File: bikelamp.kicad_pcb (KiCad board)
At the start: 2 copper layers, 44 x 46 mm, 43 parts, among them Q2 BSS138, Q3 RBFET, Q4 HIGH, Q5 LOW, Q6 ACFET, SW1 SW_MEC_5E, U1 WT51822-S4AT, U2 RUY0028A

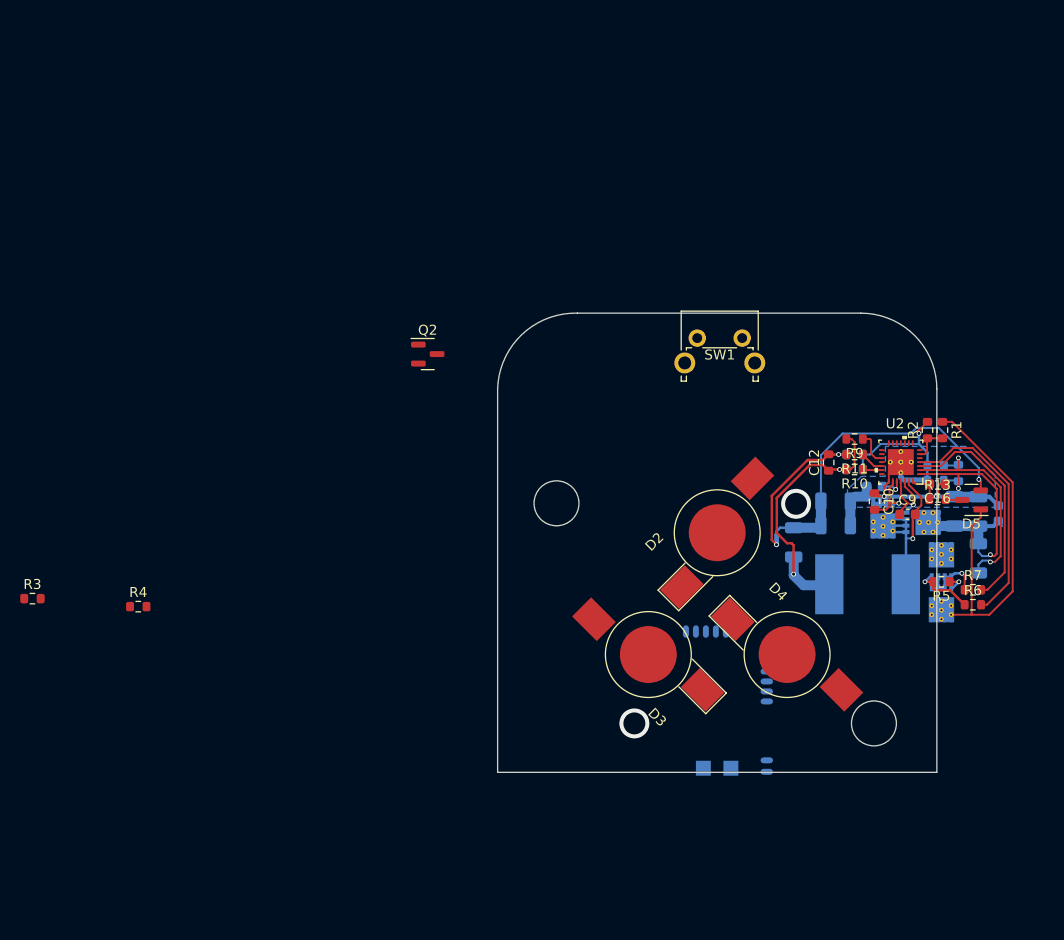
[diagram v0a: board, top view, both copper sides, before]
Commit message: Replaced BLE module with YJ-xxx
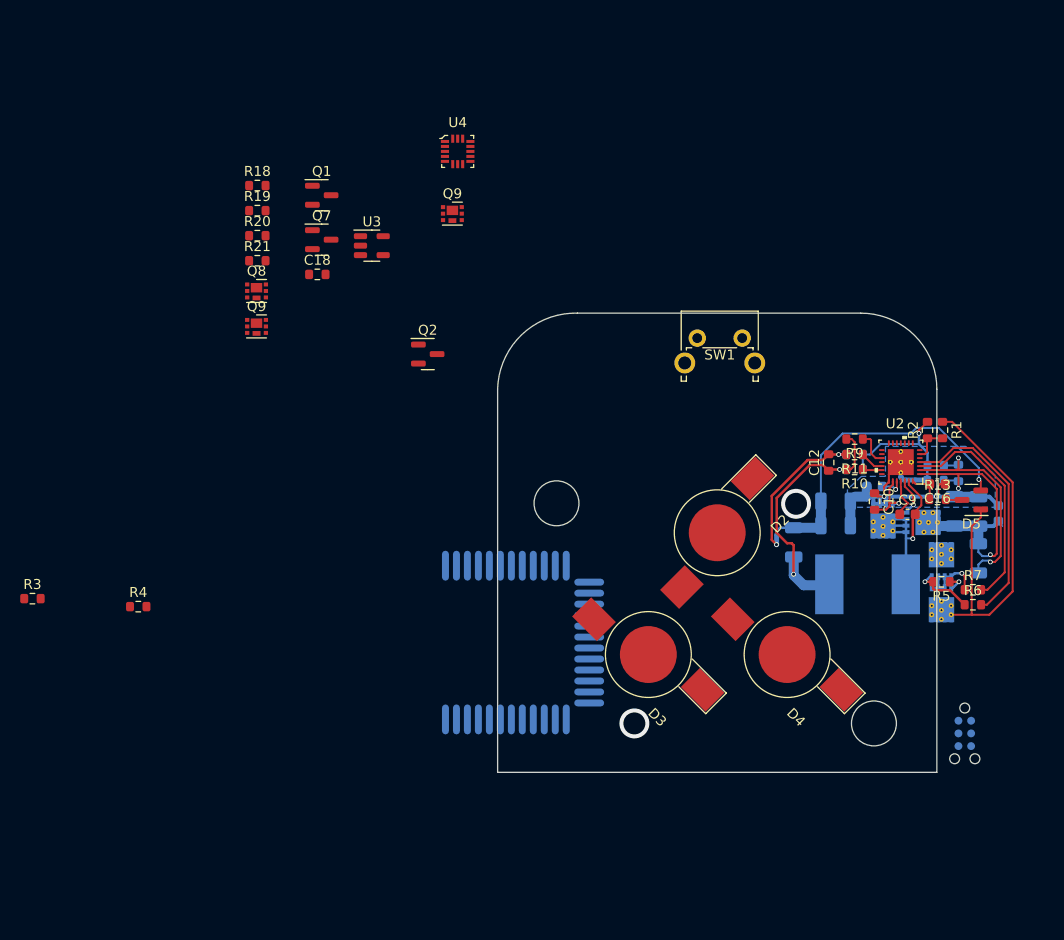
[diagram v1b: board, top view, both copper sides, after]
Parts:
- removed U1: WT51822-S4AT, libs:NRF51822-04
- added C18: 470pF, Resistor_SMD:R_0603_1608Metric, F.Cu at (-30.1, -3.88)
- added J1: Conn_ARM_SWD_TagConnect_TC2030-NL, Connector:Tag-Connect_TC2030-IDC-NL_2x03_P1.27mm_Vertical, B.Cu at (34.8, 42.1)
- added Q1: Q_PMOS_GSD, Package_TO_SOT_SMD:SOT-23, F.Cu at (-29.6, -11.8)
- added Q7: BSS138, Package_TO_SOT_SMD:SOT-23, F.Cu at (-29.6, -7.36)
- added Q8: YJQ3400A-YAN, Package_DFN_QFN:Diodes_UDFN2020-6_Type-F, F.Cu at (-36.1, -2.22)
- added Q9: YJQ3400A-YAN, Package_DFN_QFN:Diodes_UDFN2020-6_Type-F, F.Cu at (-16.5, -9.97)
- added Q9: YJQ3400A-YAN, Package_DFN_QFN:Diodes_UDFN2020-6_Type-F, F.Cu at (-36.1, 1.33)
- added R18: 100, Resistor_SMD:R_0603_1608Metric, F.Cu at (-36.1, -12.8)
- added R19: 100, Resistor_SMD:R_0603_1608Metric, F.Cu at (-36.1, -10.3)
- added R20: 100, Resistor_SMD:R_0603_1608Metric, F.Cu at (-36.1, -7.76)
- added R21: 100, Resistor_SMD:R_0603_1608Metric, F.Cu at (-36.1, -5.25)
- added U3: MIC5205-3.3YM5, Package_TO_SOT_SMD:SOT-23-5, F.Cu at (-24.6, -6.76)
- added U4: MMA8452QR1, digikey-footprints:VQFN-16_3x3mm, F.Cu at (-16.0, -16.2)
- added U5: YJ-14015, footprints:YJ-14015, B.Cu at (-22.8, 33.0)
- U2: value RUY0028A -> BQ24780SRUYR
- turned D2 to -135 degrees
- turned D4 to 135 degrees
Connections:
- net Net-(D5-Pad3) renamed /BQ24780/VCC_R
- net VIN renamed VDD
- D2 pad 1: unconnected-(D2-K) -> Net-(D2-K)
- D2 pad 2: unconnected-(D2-A) -> VBAT
- D3 pad 1: unconnected-(D3-K) -> Net-(D3-K)
- D3 pad 2: unconnected-(D3-A) -> VBAT
- D4 pad 1: unconnected-(D4-K) -> Net-(D4-K)
- D4 pad 2: unconnected-(D4-A) -> VBAT
- SW1 pad 1: unconnected-(SW1-Pad1) -> GND
- SW1 pad 2: unconnected-(SW1-Pad2) -> VBAT
- U2 pad 11: /BQ24780/SDA -> SDA
- U2 pad 12: /BQ24780/SCL -> SCL

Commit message: Working on contours
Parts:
- added C1: C_Polarized_Small, footprints:BQ24780SRUYR, F.Cu at (12.0, -17.7)
- added C19: 100nF, Capacitor_SMD:C_0603_1608Metric, F.Cu at (-1.20, -26.6)
- added C20: 5pF, Capacitor_SMD:C_0603_1608Metric, F.Cu at (-1.20, -24.1)
- added C21: 5pF, Capacitor_SMD:C_0603_1608Metric, F.Cu at (-1.20, -21.6)
- added R22: 1K, Resistor_SMD:R_0603_1608Metric, F.Cu at (-1.20, -19.1)
- added R23: 1K, Resistor_SMD:R_0603_1608Metric, F.Cu at (-1.20, -16.6)
- added R24: 47, Resistor_SMD:R_0603_1608Metric, F.Cu at (-1.20, -14.1)
- added R25: 47, Resistor_SMD:R_0603_1608Metric, F.Cu at (-1.20, -11.6)
- added U1: MCP79402T-xSN, Package_SO:SO-8_3.9x4.9mm_P1.27mm, F.Cu at (5.04, -17.3)
- added U6: MC-306, footprints:MC-306, F.Cu at (6.37, -24.2)
- C10, C11, C12, C13, C18, C3, C4, C5: footprint Resistor_SMD:R_0603_1608Metric -> Capacitor_SMD:C_0603_1608Metric
- C14, C15, C7, C8: footprint Capacitor_SMD:C_1206_3216Metric -> Capacitor_SMD:C_0603_1608Metric
- Q3, Q4, Q5, Q6: footprint libs:CSD18543Q3A -> footprints:CSD18543Q3A
- U2: value BQ24780SRUYR -> RUY0028A; footprint libs:BQ24780SRUYR -> footprints:BQ24780SRUYR
- moved J1 44.6 mm to (-9.60, 46.3), turned to 180 degrees
- moved U5 3.50 mm to (-19.5, 31.9)
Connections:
- U4 pad 11: unconnected-(U4-INT1) -> MMA8452_INT1
- U4 pad 2: unconnected-(U4-BYP) -> Net-(U4-BYP)
- U4 pad 9: unconnected-(U4-INT2) -> MMA8452_INT2
- U5 pad 14: unconnected-(U5-P00) -> LED_PWM_2
- U5 pad 15: unconnected-(U5-P01) -> LED_PWM_1
- U5 pad 16: unconnected-(U5-P02) -> LED_PWM_0
- U5 pad 17: unconnected-(U5-P03) -> WHEEL_SIGNAL
- U5 pad 19: unconnected-(U5-P05) -> SCL
- U5 pad 20: unconnected-(U5-P06) -> SDA
- U5 pad 21: unconnected-(U5-P07) -> PWR_BTN_PRESSED
- U5 pad 22: unconnected-(U5-P08) -> KEEP_POWER
- U5 pad 23: unconnected-(U5-P09) -> MMA8452_INT1
- U5 pad 24: unconnected-(U5-P10) -> MMA8452_INT2
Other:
- board size 44 x 46 mm -> 66.7 x 67.8 mm

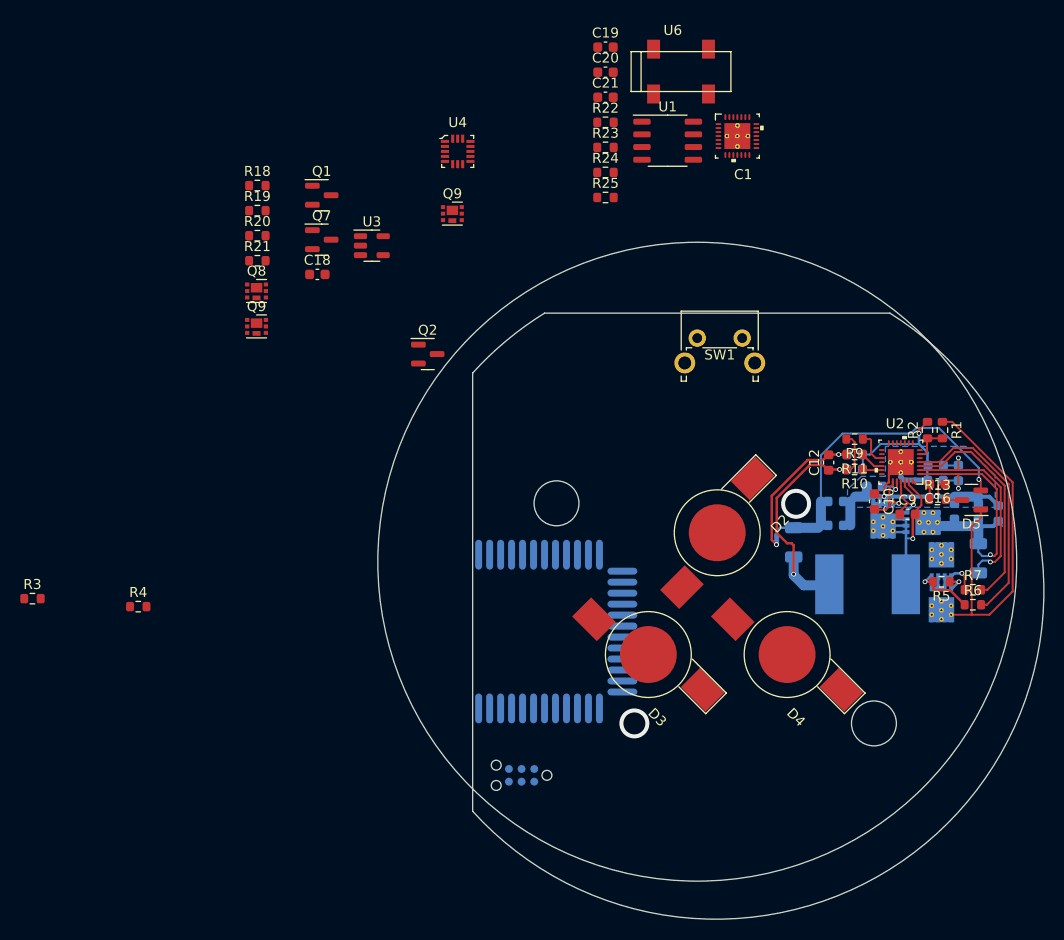
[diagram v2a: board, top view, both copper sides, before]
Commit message: Added gate protection circuit to the SCH
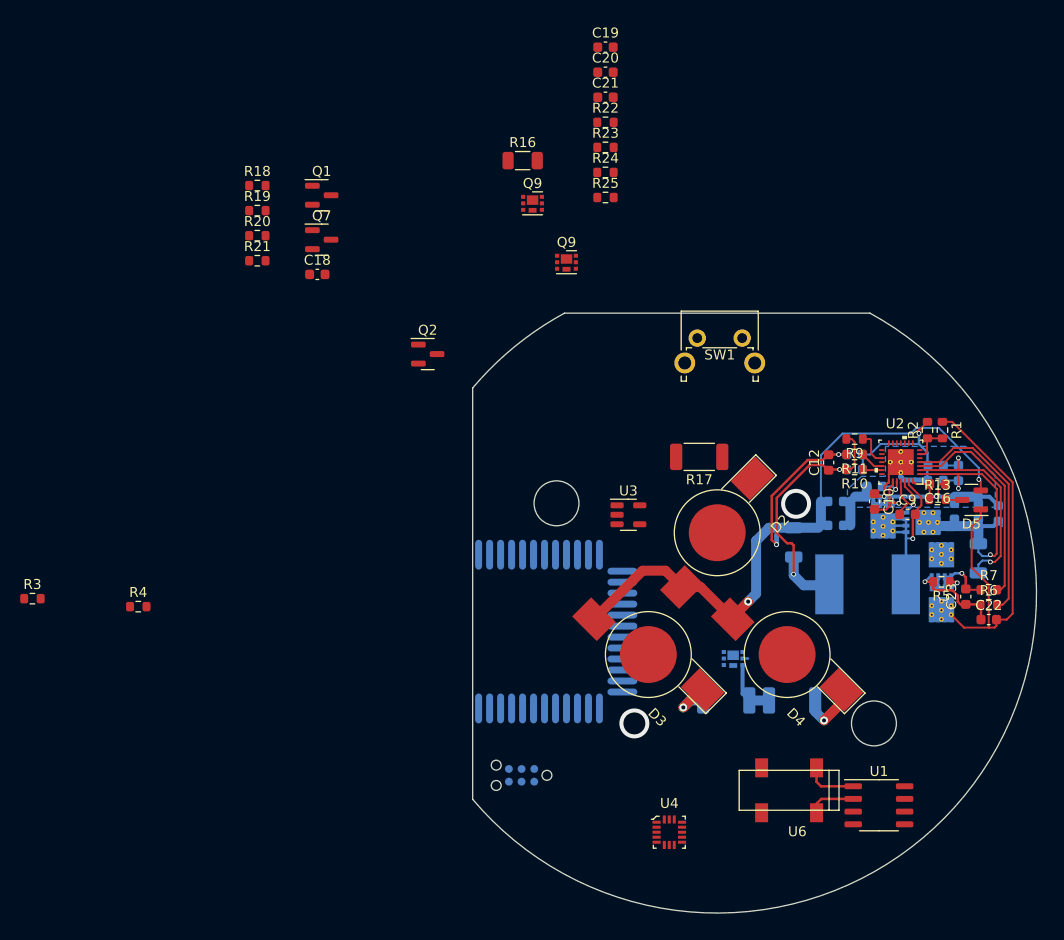
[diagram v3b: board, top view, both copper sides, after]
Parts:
- removed C1: C_Polarized_Small, footprints:BQ24780SRUYR
- added C22: 1nF, Capacitor_SMD:C_0603_1608Metric, F.Cu at (37.2, 30.7)
- added C23: 47nF, Capacitor_SMD:C_0603_1608Metric, F.Cu at (34.9, 28.4)
- added R14: TBD, Resistor_SMD:R_2010_5025Metric, B.Cu at (17.5, 38.8)
- added R15: TBD, Resistor_SMD:R_2010_5025Metric, B.Cu at (10.9, 38.8)
- added R16: TBD, Resistor_SMD:R_1206_3216Metric, F.Cu at (-9.49, -15.3)
- added R17: TBD, Resistor_SMD:R_2010_5025Metric, F.Cu at (8.20, 14.4)
- Q8: moved to B.Cu
- U2: value RUY0028A -> BQ24780SRUYR
- moved U6 72.8 mm to (17.2, 47.8), turned to 180 degrees
- moved U4 71.4 mm to (5.20, 52.0)
- moved U1 69.9 mm to (26.2, 49.3)
- moved Q8 60.3 mm to (11.6, 34.6), turned to 180 degrees
- moved U3 37.2 mm to (1.10, 20.2)
- moved Q9 31.7 mm to (-5.10, -5.10)
- moved Q9 8.10 mm to (-8.50, -11.0)
- moved R6 1.59 mm to (37.2, 29.2)
- moved R7 1.59 mm to (37.2, 27.7)
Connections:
- net ACDET renamed Net-(U2-ACDET)
- net Net-(Q8A-G) renamed /LEDs/LED1_GATE_R
- net Net-(Q8B-G) renamed /LEDs/LED2_GATE_R
- Q9 pad 1: (no net) -> GND
- Q9 pad 2: (no net) -> /LEDs/LED3_GATE_R
- Q9 pad 6: (no net) -> Net-(Q9A-D)
- Q9 pad 2: Net-(Q9A-G) -> /LEDs/LED3_GATE_R
- R20 pad 1: Net-(Q9A-G) -> /LEDs/LED3_GATE_R
- R20 pad 2: /LEDs/LED3_GATE -> LED_PWM_3
- U5 pad 18: unconnected-(U5-P04) -> LED_PWM_3
- U6 pad 1: Net-(U1-X2) -> Net-(U1-X1)
- U6 pad 4: Net-(U1-X1) -> Net-(U1-X2)
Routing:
- net VBAT: track 33.0 -> 64.1 mm, vias 1 -> 2
- net Net-(D4-K): track 0.00 -> 6.15 mm, vias 0 -> 1
- net Net-(Q8B-D): track 0.00 -> 5.80 mm
- net Net-(U1-X1): track 0.00 -> 5.26 mm
- net Net-(D3-K): track 0.00 -> 4.95 mm, vias 0 -> 1
- net Net-(U1-X2): track 0.00 -> 4.78 mm
- net VDD: track 38.5 -> 43.3 mm
- net /BQ24780/RBFET_GATE: track 6.21 -> 9.65 mm
- net /BQ24780/VIN_SWITCHABLE: track 7.78 -> 9.25 mm
- net /BQ24780/CMSRC: track 22.3 -> 21.5 mm
- net /BQ24780/ACDRV: track 24.6 -> 23.9 mm
- net /LEDs/LED1_GATE_R: track 0.00 -> 0.56 mm
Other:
- board size 66.7 x 67.8 mm -> 56.5 x 60.1 mm

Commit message: ERC pass
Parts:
- Q2: moved to B.Cu
- R3: value R_Small -> 1M; moved to B.Cu
- R4: value R_Small -> 3M; moved to B.Cu
- moved R3 98.0 mm to (39.2, 23.8), turned to 180 degrees
- moved R4 87.3 mm to (39.2, 25.3)
- moved Q2 63.0 mm to (39.2, 28.0), turned to -90 degrees
- moved R16 19.4 mm to (-7.00, 4.00)
- moved Q9 14.1 mm to (-3.00, 2.00)
- moved Q9 11.5 mm to (4.00, 2.00)
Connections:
- Q2 pad 1: unconnected-(Q2-G-Pad1) -> Net-(Q2-G)
- Q2 pad 2: unconnected-(Q2-S-Pad2) -> /BQ24780/VIN_SWITCHABLE
- Q2 pad 3: unconnected-(Q2-D-Pad3) -> /BQ24780/RBFET_GATE
- R3 pad 1: unconnected-(R3-Pad1) -> GNDPWR
- R3 pad 2: unconnected-(R3-Pad2) -> Net-(Q2-G)
- R4 pad 1: unconnected-(R4-Pad1) -> Net-(Q2-G)
- R4 pad 2: unconnected-(R4-Pad2) -> /BQ24780/VIN_SWITCHABLE
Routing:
- net /BQ24780/RBFET_GATE: track 9.65 -> 15.9 mm, vias 1 -> 2
- net GNDPWR: track 30.6 -> 36.5 mm
- net Net-(D2-K): track 0.00 -> 3.92 mm
- net Net-(Q2-G): track 0.00 -> 3.31 mm
- net /BQ24780/VIN_SWITCHABLE: track 9.25 -> 11.1 mm

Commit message: Board routed
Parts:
- removed the Q9 at (-3.00, 2.00)
- removed the Q9 at (4.00, 2.00)
- added C1: 100uF, Capacitor_SMD:CP_Elec_6.3x5.7, B.Cu at (26.3, 48.3)
- added C2: 100nF, Capacitor_SMD:C_0603_1608Metric, F.Cu at (34.1, 11.7)
- added C24: 100nF, Capacitor_SMD:C_0603_1608Metric, B.Cu at (21.2, 3.30)
- added C25: 100nF, Capacitor_SMD:C_0603_1608Metric, B.Cu at (16.0, 8.23)
- added C26: 100nF, Capacitor_SMD:C_0603_1608Metric, B.Cu at (-1.77, 21.1)
- added D1: D_Bridge_+-AA, Diode_SMD:Diode_Bridge_Diotec_ABS, B.Cu at (14.1, 45.6)
- added D6: D_Schottky, Diode_SMD:D_MicroMELF, F.Cu at (8.15, 48.1)
- added D8: BZV55C2V7, Diode_SMD:D_MiniMELF, F.Cu at (5.12, 45.1)
- added J2: Conn_01x04_Pin, Connector_Phoenix_MC:PhoenixContact_MCV_1,5_4-GF-3.5_1x04_P3.50mm_Vertical_ThreadedFlange_MountHole, B.Cu at (4.75, 52.2)
- added J_BATTERY1: Conn_01x02, Connector_JST:JST_VH_B2P-VH-FB-B_1x02_P3.96mm_Vertical, B.Cu at (35.0, 37.5)
- added Q9: YJQ3400A-YAN, footprints:DFN2020-6L, F.Cu at (15.6, 41.5)
- added R26: TBD, Resistor_SMD:R_0603_1608Metric, F.Cu at (23.4, 17.2)
- added R27: TBD, Resistor_SMD:R_0603_1608Metric, F.Cu at (23.4, 18.7)
- added R28: 10K, Resistor_SMD:R_0603_1608Metric, F.Cu at (29.1, 10.9)
- C19, C20, C21, R18, R19, U1, U6: moved to B.Cu
- L1: footprint libs:IND_ETQP5M150YFK -> Inductor_SMD:L_Bourns-SRN8040_8x8.15mm
- Q8: footprint Package_DFN_QFN:Diodes_UDFN2020-6_Type-F -> footprints:DFN2020-6L
- U4: footprint digikey-footprints:VQFN-16_3x3mm -> footprints:VQFN-16_3x3mm; moved to B.Cu
- moved R21 71.9 mm to (18.6, 41.5)
- moved R20 69.3 mm to (11.9, 42.3), turned to 180 degrees
- moved R18 69.3 mm to (14.5, 34.6)
- moved R22 66.9 mm to (5.65, 47.4)
- moved R23 64.1 mm to (2.60, 47.4)
- moved R19 63.3 mm to (8.62, 34.6), turned to 180 degrees
- moved U4 51.0 mm to (23.9, 4.58), turned to 180 degrees
- moved R16 48.2 mm to (15.3, 46.7), turned to 90 degrees
- moved Q1 42.6 mm to (1.35, 17.4), turned to -90 degrees
- moved C19 42.2 mm to (27.1, 4.67), turned to 90 degrees
- moved C21 39.7 mm to (8.09, 17.0), turned to 90 degrees
- moved U1 38.9 mm to (16.0, 11.8)
- moved C18 38.7 mm to (-0.07, 20.5), turned to 180 degrees
- moved Q7 37.3 mm to (1.35, 13.4), turned to -90 degrees
- moved U6 36.0 mm to (6.99, 13.3)
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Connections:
- net /BQ24780/ACN renamed /BQ24780/VIN_I_MEASURED
- net /BQ24780/ACP renamed /BQ24780/VIN_REVPROT
- R16 pad 1: Net-(J_REAR_LAMP1-Pin_1) -> REAR_LAMP_K
- U2 pad 10: unconnected-(U2-PROCHOT_N-Pad10) -> Net-(U2-PROCHOT_N)
- U2 pad 13: unconnected-(U2-CMPIN-Pad13) -> GND
- U2 pad 15: unconnected-(U2-BATPRES_N-Pad15) -> GND
- U2 pad 16: unconnected-(U2-TB_STAT_N-Pad16) -> TB_STAT
- U2 pad 21: unconnected-(U2-ILIM-Pad21) -> /BQ24780/ILIM
- U2 pad 5: unconnected-(U2-ACOK-Pad5) -> ACOK
- U5 pad 15: LED_PWM_1 -> LED_PWM_0
- U5 pad 16: LED_PWM_0 -> LED_PWM_1
- U5 pad 17: WHEEL_SIGNAL -> unconnected-(U5-P03-Pad17)
- U5 pad 25: unconnected-(U5-P11-Pad25) -> TB_STAT
- U5 pad 26: unconnected-(U5-P12-Pad26) -> ACOK
- U5 pad 27: unconnected-(U5-P13-Pad27) -> WHEEL_SIGNAL
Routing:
- net GND: track 15.3 -> 307.7 mm, vias 1 -> 12
- net +3V3: track 0.00 -> 141.1 mm, vias 0 -> 8
- net ACOK: track 0.00 -> 104.3 mm, vias 0 -> 3
- net VBAT: track 64.1 -> 168.1 mm, vias 2 -> 4
- net SCL: track 0.00 -> 98.8 mm, vias 0 -> 3
- net MMA8452_INT2: track 0.00 -> 88.8 mm, vias 0 -> 2
- net TB_STAT: track 0.00 -> 83.3 mm, vias 0 -> 3
- net SDA: track 0.00 -> 77.6 mm, vias 0 -> 3
- net MMA8452_INT1: track 0.00 -> 74.9 mm, vias 0 -> 2
- net VDD: track 43.3 -> 80.9 mm, vias 0 -> 1
- net KEEP_POWER: track 0.00 -> 35.0 mm, vias 0 -> 1
- net LED_PWM_2: track 0.00 -> 34.5 mm, vias 0 -> 1
- net Net-(Q8A-D): track 0.00 -> 30.8 mm, vias 0 -> 1
- net LED_PWM_0: track 0.00 -> 18.4 mm
- net LED_PWM_3: track 0.00 -> 18.1 mm, vias 0 -> 1
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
